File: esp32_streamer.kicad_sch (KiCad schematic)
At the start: 44 parts, among them J1 USB4510-03-1-A, J2 SJ1-3533NS, J3 Conn_01x04_Male, U1 PCM5122PW, U2 ESP32-WROVER-EM213EH2864PH3Q0, U3 MCP1825S, U4 MCP1825S

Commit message: Sensible changes to grid and component placement for DAC (following TI datasheet)
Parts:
- C3, C4: value 2.2uF UUQ1H2R2MCL1GB -> 2.2uF
- J3: footprint Connector_PinHeader_2.54mm:PinHeader_1x04_P2.54mm_Horizontal -> Connector_PinHeader_2.54mm:PinHeader_1x04_P2.54mm_Vertical
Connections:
- net GND: now also C4.1; no longer C4.2
- net VNEG: now reaches U1.5 (VNEG)
- net VNEG: now also C4.2; no longer C4.1
- net LDO0: now reaches C7.1, C8.1, U1.26 (LDOO)
- net JACKR: now reaches C2.1, J2.3, R5.2
- net OUTR: now reaches R5.1, U1.7 (OUTR)
- net XSMT: now reaches R7.2, U1.25 (XSMT)
- net DEMP: now reaches R6.1, U1.10 (VCOM/DEMP)
- net CAPP: now reaches C3.1, U1.2 (CAPP)
- net CAPM: now reaches C3.2, U1.4 (CAPM)
- net OUTL: now reaches R4.2, U1.6 (OUTL)
- net JACKL: now reaches C1.2, J2.2, R4.1
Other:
- moved on the sheet: C4, R7
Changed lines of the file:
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@@
     (stroke (width 0) (type default) (color 0 0 0 0))
   )
-  (wire (pts (xy 167.64 82.55) (xy 171.45 82.55))
+  (wire (pts (xy 167.64 82.55) (xy 168.91 82.55))
     (stroke (width 0) (type default) (color 0 0 0 0))
   )
@@
   )
   (wire (pts (xy 175.26 132.08) (xy 173.99 132.08))
+    (stroke (width 0) (type default) (color 0 0 0 0))
+  )
+  (wire (pts (xy 217.17 82.55) (xy 223.52 82.55))
     (stroke (width 0) (type default) (color 0 0 0 0))
   )
@@
     (stroke (width 0) (type default) (color 0 0 0 0))
   )
+  (wire (pts (xy 223.52 91.44) (xy 223.52 90.17))
+    (stroke (width 0) (type default) (color 0 0 0 0))
+  )
   (wire (pts (xy 222.25 74.93) (xy 222.25 77.47))
     (stroke (width 0) (type default) (color 0 0 0 0))
@@
     (stroke (width 0) (type default) (color 0 0 0 0))
   )
-  (wire (pts (xy 217.17 82.55) (xy 223.52 82.55))
-    (stroke (width 0) (type default) (color 0 0 0 0))
-  )
   (wire (pts (xy 90.17 24.13) (xy 81.28 24.13))
     (stroke (width 0) (type default) (color 0 0 0 0))
@@
     (stroke (width 0) (type default) (color 0 0 0 0))
   )
-  (wire (pts (xy 179.07 82.55) (xy 181.61 82.55))
+  (wire (pts (xy 176.53 82.55) (xy 181.61 82.55))
     (stroke (width 0) (type default) (color 0 0 0 0))
   )
@@
     (effects (font (size 1.27 1.27) (thickness 0.254) bold) (justify left bottom))
   )
+  (label "CAPP" (at 217.17 72.39 0)
+    (effects (font (size 1.27 1.27)) (justify left bottom))
+  )
   (label "GPIO12" (at 24.13 72.39 0)
     (effects (font (size 1.27 1.27)) (justify left bottom))
   )
   (label "VBUS_RP" (at 208.28 113.03 0)
+    (effects (font (size 1.27 1.27)) (justify left bottom))
+  )
+  (label "OUTL" (at 219.71 46.99 0)
+    (effects (font (size 1.27 1.27)) (justify left bottom))
+  )
+  (label "JACKL" (at 242.57 46.99 0)
+    (effects (font (size 1.27 1.27)) (justify left bottom))
+  )
+  (label "DEMP" (at 217.17 67.31 0)
+    (effects (font (size 1.27 1.27)) (justify left bottom))
+  )
+  (label "JACKR" (at 242.57 49.53 0)
+    (effects (font (size 1.27 1.27)) (justify left bottom))
+  )
+  (label "OUTR" (at 219.71 49.53 0)
+    (effects (font (size 1.27 1.27)) (justify left bottom))
+  )
+  (label "VNEG" (at 217.17 82.55 0)
+    (effects (font (size 1.27 1.27)) (justify left bottom))
+  )
+  (label "CAPM" (at 217.17 74.93 0)
+    (effects (font (size 1.27 1.27)) (justify left bottom))
+  )
+  (label "XSMT" (at 176.53 82.55 0)
+    (effects (font (size 1.27 1.27)) (justify left bottom))
+  )
+  (label "LDO0" (at 217.17 80.01 0)
     (effects (font (size 1.27 1.27)) (justify left bottom))
   )
@@
     (pin "2")
   )
-  (symbol (lib_name "UUQ1H2R2MCL1GB_1") (lib_id "Nichicon UUQ1H2R2MCL1GB:UUQ1H2R2MCL1GB") (at 223.52 82.55 270) (unit 1)
-    (in_bom yes) (on_board yes)
-    (property "Reference" "C4" (id 0) (at 227.33 86.36 90)
+  (symbol (lib_name "UUQ1H2R2MCL1GB_1") (lib_id "Nichicon UUQ1H2R2MCL1GB:UUQ1H2R2MCL1GB") (at 223.52 90.17 90) (unit 1)
+    (in_bom yes) (on_board yes)
+    (property "Reference" "C4" (id 0) (at 219.71 86.36 90)
       (effects (font (size 1.524 1.524)) (justify left))
     )
-    (property "Value" "2.2uF UUQ1H2R2MCL1GB" (id 1) (at 226.06 83.82 90)
+    (property "Value" "2.2uF" (id 1) (at 232.41 86.36 90)
       (effects (font (size 1.524 1.524)) (justify left))
     )
-    (property "Footprint" "library:UUQ1H2R2MCL1GB" (id 2) (at 219.71 73.406 0)
+    (property "Footprint" "library:UUQ1H2R2MCL1GB" (id 2) (at 227.33 99.314 0)
       (effects (font (size 1.524 1.524)) hide)
     )
-    (property "Datasheet" "" (id 3) (at 223.52 82.55 0)
+    (property "Datasheet" "" (id 3) (at 223.52 90.17 0)
       (effects (font (size 1.524 1.524)))
     )
@@
     (pin "1")
   )
-  (symbol (lib_id "power:GND") (at 223.52 90.17 0) (unit 1)
-    (in_bom yes) (on_board yes) (fields_autoplaced)
-    (property "Reference" "#PWR0118" (id 0) (at 223.52 96.52 0)
-      (effects (font (size 1.27 1.27)) hide)
-    )
-    (property "Value" "GND" (id 1) (at 223.52 95.25 0))
-    (property "Footprint" "" (id 2) (at 223.52 90.17 0)
-      (effects (font (size 1.27 1.27)) hide)
-    )
-    (property "Datasheet" "" (id 3) (at 223.52 90.17 0)
+  (symbol (lib_id "power:GND") (at 223.52 91.44 0) (unit 1)
+    (in_bom yes) (on_board yes) (fields_autoplaced)
+    (property "Reference" "#PWR0118" (id 0) (at 223.52 97.79 0)
+      (effects (font (size 1.27 1.27)) hide)
+    )
+    (property "Value" "GND" (id 1) (at 223.52 96.52 0))
+    (property "Footprint" "" (id 2) (at 223.52 91.44 0)
+      (effects (font (size 1.27 1.27)) hide)
+    )
+    (property "Datasheet" "" (id 3) (at 223.52 91.44 0)
       (effects (font (size 1.27 1.27)) hide)
     )
@@
     (pin "4")
   )
-  (symbol (lib_id "Device:R") (at 175.26 82.55 90) (unit 1)
-    (in_bom yes) (on_board yes)
-    (property "Reference" "R7" (id 0) (at 175.26 85.09 90))
-    (property "Value" "1kΩ" (id 1) (at 175.26 87.63 90))
-    (property "Footprint" "Resistor_SMD:R_0603_1608Metric" (id 2) (at 175.26 84.328 90)
-      (effects (font (size 1.27 1.27)) hide)
-    )
-    (property "Datasheet" "" (id 3) (at 175.26 82.55 0)
+  (symbol (lib_id "Device:R") (at 172.72 82.55 90) (unit 1)
+    (in_bom yes) (on_board yes)
+    (property "Reference" "R7" (id 0) (at 172.72 85.09 90))
+    (property "Value" "1kΩ" (id 1) (at 172.72 87.63 90))
+    (property "Footprint" "Resistor_SMD:R_0603_1608Metric" (id 2) (at 172.72 84.328 90)
+      (effects (font (size 1.27 1.27)) hide)
+    )
+    (property "Datasheet" "" (id 3) (at 172.72 82.55 0)
       (effects (font (size 1.27 1.27)) hide)
     )
@@
     (property "Reference" "J3" (id 0) (at 28.575 24.13 0))
     (property "Value" "Conn_01x04_Male" (id 1) (at 28.575 26.67 0))
-    (property "Footprint" "Connector_PinHeader_2.54mm:PinHeader_1x04_P2.54mm_Horizontal" (id 2) (at 27.94 31.75 0)
+    (property "Footprint" "Connector_PinHeader_2.54mm:PinHeader_1x04_P2.54mm_Vertical" (id 2) (at 27.94 31.75 0)
       (effects (font (size 1.27 1.27)) hide)
     )
@@
       (effects (font (size 1.524 1.524)) (justify left))
     )
-    (property "Value" "2.2uF UUQ1H2R2MCL1GB" (id 1) (at 234.95 73.66 90)
+    (property "Value" "2.2uF" (id 1) (at 229.87 76.2 90)
       (effects (font (size 1.524 1.524)) (justify left))
     )
@@
     )
     (path "/e5dee374-867d-47f7-b303-ef0dc4f66b9a"
-      (reference "C3") (unit 1) (value "2.2uF UUQ1H2R2MCL1GB") (footprint "library:UUQ1H2R2MCL1GB")
+      (reference "C3") (unit 1) (value "2.2uF") (footprint "library:UUQ1H2R2MCL1GB")
     )
     (path "/26d954a7-0a59-494a-8b0d-045bf59a826e"
-      (reference "C4") (unit 1) (value "2.2uF UUQ1H2R2MCL1GB") (footprint "library:UUQ1H2R2MCL1GB")
+      (reference "C4") (unit 1) (value "2.2uF") (footprint "library:UUQ1H2R2MCL1GB")
     )
     (path "/0939bf1c-3b01-4a1d-a6fe-f5720dfc5d1d"
@@
     )
     (path "/b2ba889e-fe8d-4a7a-bd26-c7dd5196d6eb"
-      (reference "J3") (unit 1) (value "Conn_01x04_Male") (footprint "Connector_PinHeader_2.54mm:PinHeader_1x04_P2.54mm_Horizontal")
+      (reference "J3") (unit 1) (value "Conn_01x04_Male") (footprint "Connector_PinHeader_2.54mm:PinHeader_1x04_P2.54mm_Vertical")
     )
     (path "/3ed27af6-816a-449b-9b7e-3150878e8ddc"

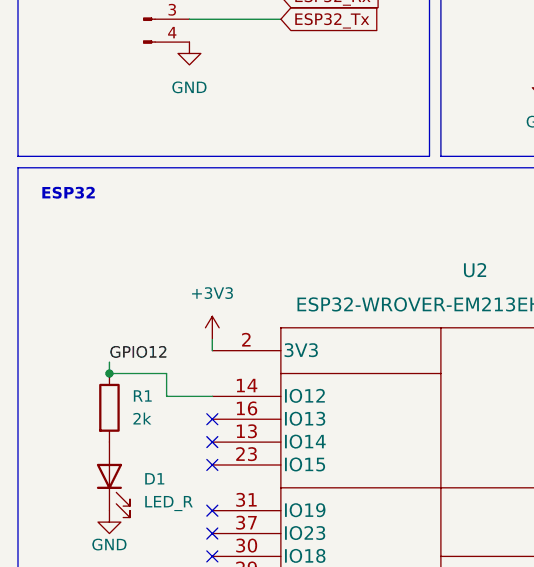
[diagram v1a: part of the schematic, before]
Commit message: Analog DAC components now laid out properly (hopefully).
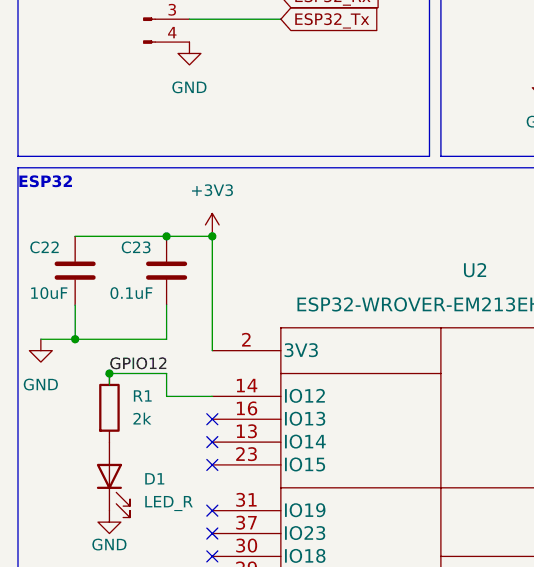
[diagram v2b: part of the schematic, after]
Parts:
- added C22: 10uF, Capacitor_SMD:C_1206_3216Metric, symbol Device:C
- added C23: 0.1uF, Capacitor_SMD:C_0805_2012Metric, symbol Device:C
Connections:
- net +3V3: now also C22.1, C23.1
- net GND: now also C22.2, C23.2
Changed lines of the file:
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@@
   (junction (at 213.36 115.57) (diameter 0) (color 0 0 0 0)
   )
+  (junction (at 35.56 58.42) (diameter 0) (color 0 0 0 0)
+  )
   (junction (at 199.39 22.86) (diameter 0) (color 0 0 0 0)
   )
@@
   (junction (at 237.49 62.23) (diameter 0) (color 0 0 0 0)
   )
+  (junction (at 30.48 58.42) (diameter 0) (color 0 0 0 0)
+  )
   (junction (at 173.99 134.62) (diameter 0) (color 0 0 0 0)
   )
@@
   )
   (junction (at 262.89 130.81) (diameter 0) (color 0 0 0 0)
+  )
+  (junction (at 20.32 69.85) (diameter 0) (color 0 0 0 0)
   )
   (junction (at 130.81 24.13) (diameter 0) (color 0 0 0 0)
@@
     (stroke (width 0) (type default) (color 0 0 0 0))
   )
+  (wire (pts (xy 20.32 69.85) (xy 16.51 69.85))
+    (stroke (width 0) (type default) (color 0 0 0 0))
+  )
   (wire (pts (xy 262.89 130.81) (xy 262.89 133.35))
     (stroke (width 0) (type default) (color 0 0 0 0))
@@
     (stroke (width 0) (type default) (color 0 0 0 0))
   )
+  (wire (pts (xy 30.48 58.42) (xy 35.56 58.42))
+    (stroke (width 0) (type default) (color 0 0 0 0))
+  )
   (wire (pts (xy 201.93 87.63) (xy 201.93 91.44))
     (stroke (width 0) (type default) (color 0 0 0 0))
@@
     (stroke (width 0) (type default) (color 0 0 0 0))
   )
+  (wire (pts (xy 20.32 69.85) (xy 30.48 69.85))
+    (stroke (width 0) (type default) (color 0 0 0 0))
+  )
   (wire (pts (xy 199.39 87.63) (xy 199.39 91.44))
     (stroke (width 0) (type default) (color 0 0 0 0))
@@
     (stroke (width 0) (type default) (color 0 0 0 0))
   )
+  (wire (pts (xy 20.32 66.04) (xy 20.32 69.85))
+    (stroke (width 0) (type default) (color 0 0 0 0))
+  )
   (wire (pts (xy 270.51 80.01) (xy 257.81 80.01))
     (stroke (width 0) (type default) (color 0 0 0 0))
@@
     (stroke (width 0) (type default) (color 0 0 0 0))
   )
-  (wire (pts (xy 35.56 69.85) (xy 35.56 71.12))
+  (wire (pts (xy 35.56 58.42) (xy 35.56 71.12))
     (stroke (width 0) (type default) (color 0 0 0 0))
   )
@@
     (stroke (width 0) (type default) (color 0 0 0 0))
   )
+  (wire (pts (xy 30.48 66.04) (xy 30.48 69.85))
+    (stroke (width 0) (type default) (color 0 0 0 0))
+  )
   (wire (pts (xy 233.68 46.99) (xy 237.49 46.99))
     (stroke (width 0) (type default) (color 0 0 0 0))
@@
     (stroke (width 0) (type default) (color 0 0 0 0))
   )
+  (wire (pts (xy 20.32 58.42) (xy 30.48 58.42))
+    (stroke (width 0) (type default) (color 0 0 0 0))
+  )
   (wire (pts (xy 137.16 123.19) (xy 142.24 123.19))
     (stroke (width 0) (type default) (color 0 0 0 0))
@@
     (stroke (width 0) (type default) (color 0 0 0 0))
   )
+  (wire (pts (xy 24.13 74.93) (xy 24.13 73.66))
+    (stroke (width 0) (type default) (color 0 0 0 0))
+  )
   (wire (pts (xy 208.28 115.57) (xy 213.36 115.57))
     (stroke (width 0) (type default) (color 0 0 0 0))
@@
   )
   (wire (pts (xy 231.14 115.57) (xy 236.22 115.57))
-    (stroke (width 0) (type default) (color 0 0 0 0))
-  )
-  (wire (pts (xy 24.13 72.39) (xy 24.13 73.66))
     (stroke (width 0) (type default) (color 0 0 0 0))
   )
@@
     (effects (font (size 1.27 1.27) (thickness 0.254) bold) (justify left bottom))
   )
-  (text "ESP32" (at 16.51 54.61 0)
+  (text "ESP32" (at 13.97 53.34 0)
     (effects (font (size 1.27 1.27) (thickness 0.254) bold) (justify left bottom))
   )
@@
     (effects (font (size 1.27 1.27)) (justify left bottom))
   )
-  (label "GPIO12" (at 24.13 72.39 0)
+  (label "GPIO12" (at 24.13 73.66 0)
     (effects (font (size 1.27 1.27)) (justify left bottom))
   )
@@
     (pin "2")
   )
-  (symbol (lib_id "power:+3V3") (at 35.56 69.85 0) (unit 1)
-    (in_bom yes) (on_board yes) (fields_autoplaced)
-    (property "Reference" "#PWR0128" (id 0) (at 35.56 73.66 0)
-      (effects (font (size 1.27 1.27)) hide)
-    )
-    (property "Value" "+3V3" (id 1) (at 35.56 64.77 0))
-    (property "Footprint" "" (id 2) (at 35.56 69.85 0)
-      (effects (font (size 1.27 1.27)) hide)
-    )
-    (property "Datasheet" "" (id 3) (at 35.56 69.85 0)
+  (symbol (lib_id "power:+3V3") (at 35.56 58.42 0) (unit 1)
+    (in_bom yes) (on_board yes) (fields_autoplaced)
+    (property "Reference" "#PWR0128" (id 0) (at 35.56 62.23 0)
+      (effects (font (size 1.27 1.27)) hide)
+    )
+    (property "Value" "+3V3" (id 1) (at 35.56 53.34 0))
+    (property "Footprint" "" (id 2) (at 35.56 58.42 0)
+      (effects (font (size 1.27 1.27)) hide)
+    )
+    (property "Datasheet" "" (id 3) (at 35.56 58.42 0)
       (effects (font (size 1.27 1.27)) hide)
     )
@@
     )
     (property "Datasheet" "" (id 3) (at 107.95 116.84 0)
+      (effects (font (size 1.27 1.27)) hide)
+    )
+    (pin "1")
+    (pin "2")
+  )
+  (symbol (lib_id "Device:C") (at 20.32 62.23 0) (unit 1)
+    (in_bom yes) (on_board yes)
+    (property "Reference" "C22" (id 0) (at 15.24 59.69 0)
+      (effects (font (size 1.27 1.27)) (justify left))
+    )
+    (property "Value" "10uF" (id 1) (at 15.24 64.77 0)
+      (effects (font (size 1.27 1.27)) (justify left))
+    )
+    (property "Footprint" "Capacitor_SMD:C_1206_3216Metric" (id 2) (at 21.2852 66.04 0)
+      (effects (font (size 1.27 1.27)) hide)
+    )
+    (property "Datasheet" "~" (id 3) (at 20.32 62.23 0)
       (effects (font (size 1.27 1.27)) hide)
     )
@@
     (pin "2")
   )
+  (symbol (lib_id "power:GND") (at 16.51 69.85 0) (unit 1)
+    (in_bom yes) (on_board yes) (fields_autoplaced)
+    (property "Reference" "#PWR03" (id 0) (at 16.51 76.2 0)
+      (effects (font (size 1.27 1.27)) hide)
+    )
+    (property "Value" "GND" (id 1) (at 16.51 74.93 0))
+    (property "Footprint" "" (id 2) (at 16.51 69.85 0)
+      (effects (font (size 1.27 1.27)) hide)
+    )
+    (property "Datasheet" "" (id 3) (at 16.51 69.85 0)
+      (effects (font (size 1.27 1.27)) hide)
+    )
+    (pin "1")
+  )
   (symbol (lib_id "Device:LED") (at 24.13 85.09 90) (unit 1)
     (in_bom yes) (on_board yes) (fields_autoplaced)
@@
     )
     (property "Datasheet" "~" (id 3) (at 24.13 85.09 0)
+      (effects (font (size 1.27 1.27)) hide)
+    )
+    (pin "1")
+    (pin "2")
+  )
+  (symbol (lib_id "Device:C") (at 30.48 62.23 0) (unit 1)
+    (in_bom yes) (on_board yes)
+    (property "Reference" "C23" (id 0) (at 25.4 59.69 0)
+      (effects (font (size 1.27 1.27)) (justify left))
+    )
+    (property "Value" "0.1uF" (id 1) (at 24.13 64.77 0)
+      (effects (font (size 1.27 1.27)) (justify left))
+    )
+    (property "Footprint" "Capacitor_SMD:C_0805_2012Metric" (id 2) (at 31.4452 66.04 0)
+      (effects (font (size 1.27 1.27)) hide)
+    )
+    (property "Datasheet" "~" (id 3) (at 30.48 62.23 0)
       (effects (font (size 1.27 1.27)) hide)
     )
@@
       (reference "#PWR02") (unit 1) (value "GND") (footprint "")
     )
+    (path "/e797ab51-de67-4bf9-a2b8-6b1148adcdd0"
+      (reference "#PWR03") (unit 1) (value "GND") (footprint "")
+    )
     (path "/ae4f5575-0b3a-49e2-b04d-0625b89638cc"
       (reference "#PWR0101") (unit 1) (value "GND") (footprint "")
@@
       (reference "C21") (unit 1) (value "0.1uF") (footprint "Capacitor_SMD:C_0805_2012Metric")
     )
+    (path "/a16ec7e4-2de0-4efa-80aa-5d09fd9356e9"
+      (reference "C22") (unit 1) (value "10uF") (footprint "Capacitor_SMD:C_1206_3216Metric")
+    )
+    (path "/e923b72c-c467-4552-ac38-5823717c6ea0"
+      (reference "C23") (unit 1) (value "0.1uF") (footprint "Capacitor_SMD:C_0805_2012Metric")
+    )
     (path "/e821f9b8-2ba8-4155-9437-1f1fda29defa"
